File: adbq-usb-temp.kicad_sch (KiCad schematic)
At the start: 72 parts, among them J4 USB_C_Receptacle_USB2.0_14P, Q1 Q_NMOS, Q2 Q_NMOS, Q3 Q_NMOS, SW1 SW_Push, SW2 TestPoint, SW3 TestPoint, SW4 TestPoint, U1 ESP32-S3FH4R2, U14 TMP117AIDRV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

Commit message: schem: run and fix ERC
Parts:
- L1: value L -> 0u47
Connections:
- net DIG1: now also U1.16 (GPIO11/ADC2_CH0)
- net DIG2: now also U1.17 (GPIO12/ADC2_CH1)
- net DIG3: now also U1.18 (GPIO13/ADC2_CH2)

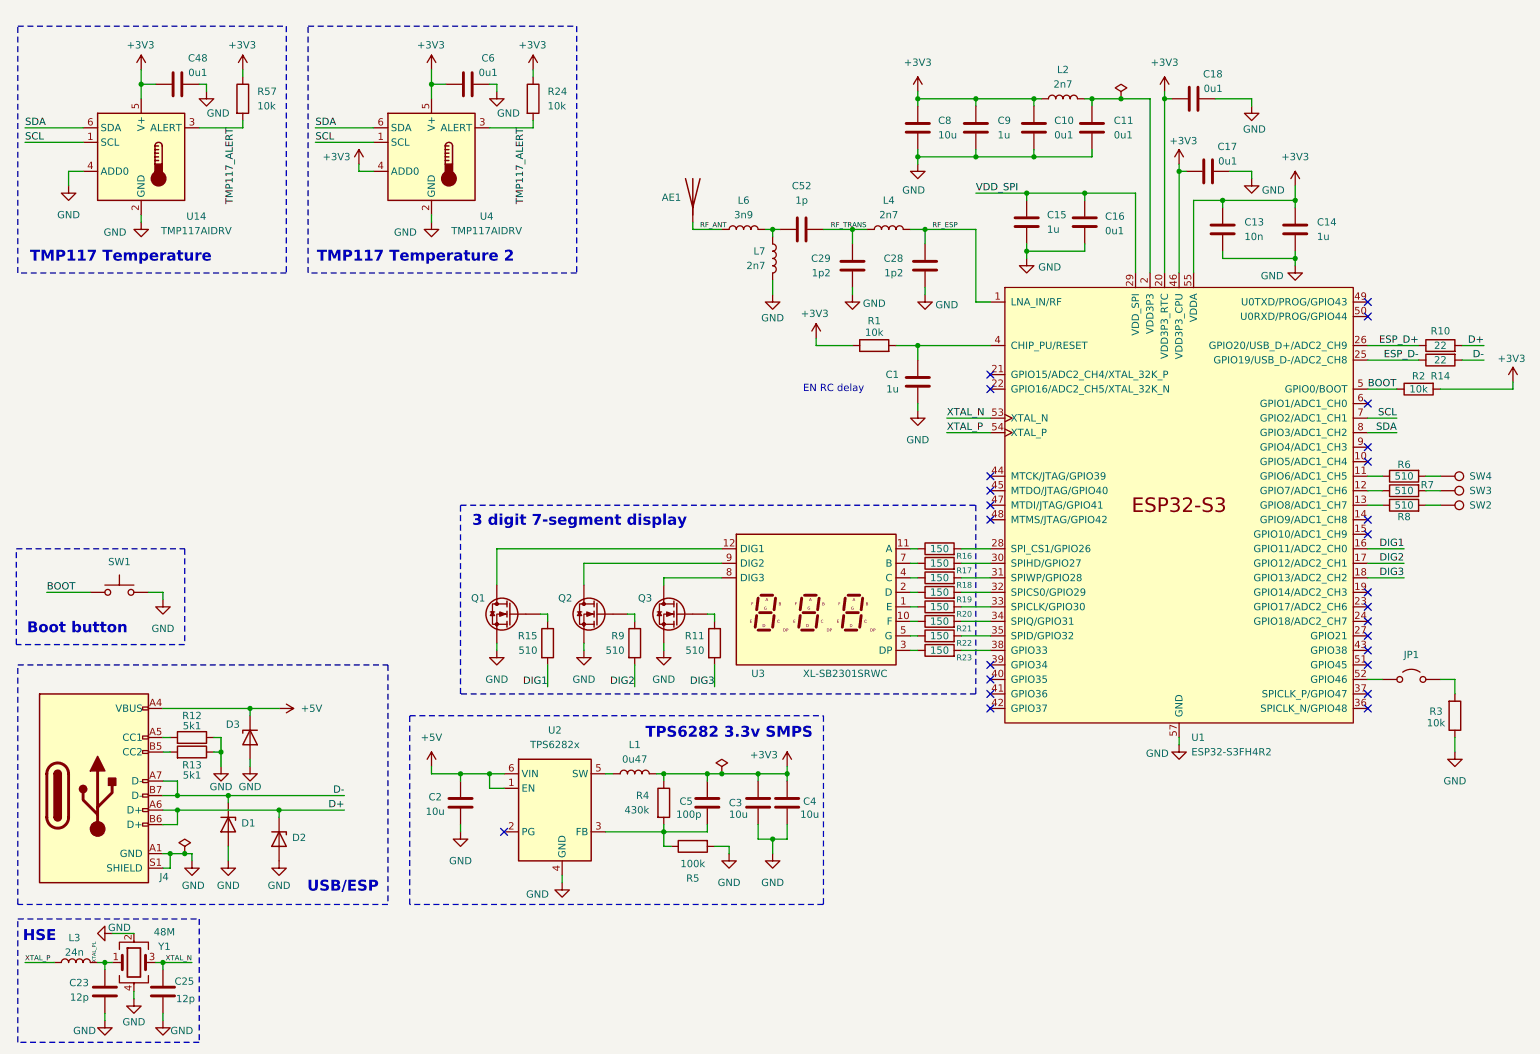
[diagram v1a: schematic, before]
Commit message: schem: add i2c pullup
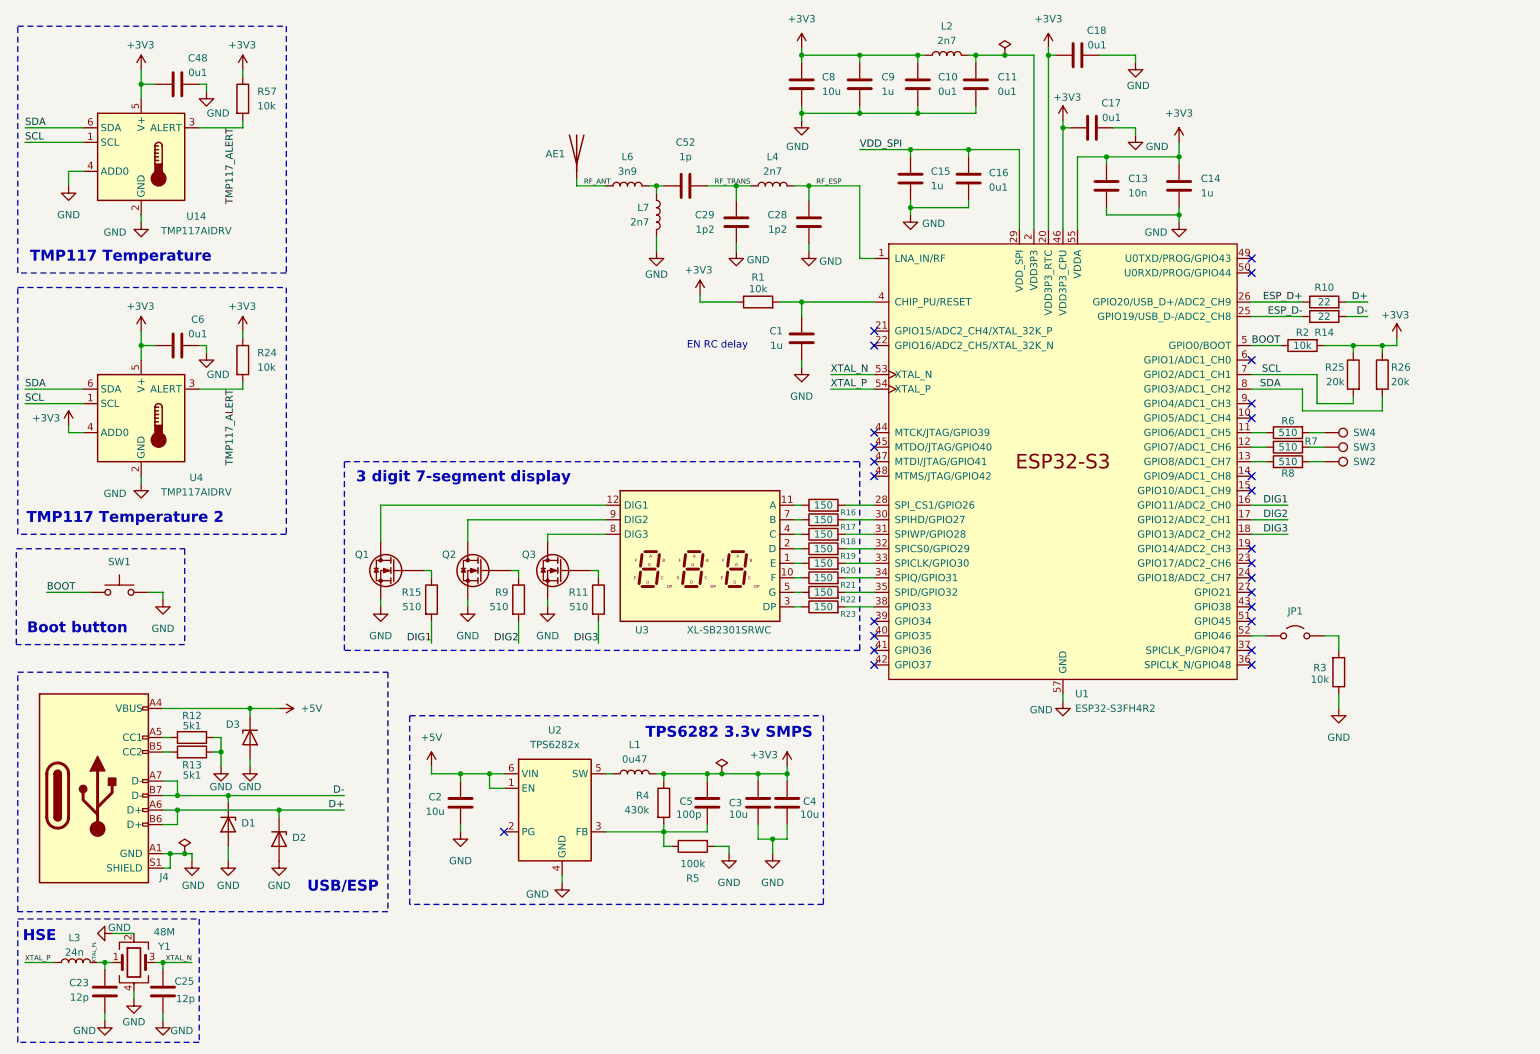
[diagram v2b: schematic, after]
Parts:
- added R25, R26: 20k, symbol Device:R
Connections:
- net +3V3: now also R25.1, R26.1
- net SCL: now also R25.2
- net SDA: now also R26.2
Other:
- moved on the sheet: AE1, C1, C10, C11, C13, C14, C15, C16, C17, C18, C28, C29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

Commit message: schem: connect TMP117 altert pins to MCU
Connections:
- net TMP117_ALERT: now also U1.24 (GPIO18/ADC2_CH7); no longer R24.2, U4.3 (ALERT)
- net TMP117_ALERT_2: now reaches U1.23 (GPIO17/ADC2_CH6)
- net TMP117_ALERT_2: now also R24.2, U4.3 (ALERT)
- no-connect marks 26 -> 24
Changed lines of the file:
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@@
-	)
-	(no_connect
-		(at 232.41 113.03)
 	)
 	(no_connect
@@
 	)
 	(no_connect
-		(at 232.41 110.49)
-	)
-	(no_connect
 		(at 232.41 115.57)
 	)
@@
 	(wire
 		(pts
+			(xy 232.41 113.03) (xy 250.19 113.03)
+		)
+		(stroke
+			(width 0)
+			(type default)
+		)
+	)
+	(wire
+		(pts
 			(xy 49.53 73.66) (xy 49.53 72.39)
 		)
@@
 		(pts
 			(xy 129.54 147.32) (xy 137.16 147.32)
+		)
+		(stroke
+			(width 0)
+			(type default)
+		)
+	)
+	(wire
+		(pts
+			(xy 232.41 110.49) (xy 250.19 110.49)
 		)
 		(stroke
@@
 		)
 	)
+	(label "TMP117_ALERT"
+		(at 250.19 113.03 180)
+		(effects
+			(font
+				(size 1.27 1.27)
+			)
+			(justify right bottom)
+		)
+	)
 	(label "SDA"
 		(at 17.78 80.01 0)
@@
 		)
 	)
+	(label "TMP117_ALERT_2"
+		(at 250.19 110.49 180)
+		(effects
+			(font
+				(size 1.27 1.27)
+			)
+			(justify right bottom)
+		)
+	)
 	(label "DIG1"
 		(at 88.9 124.46 180)
@@
 		)
 	)
-	(label "TMP117_ALERT"
+	(label "TMP117_ALERT_2"
 		(at 54.61 80.01 270)
 		(effects

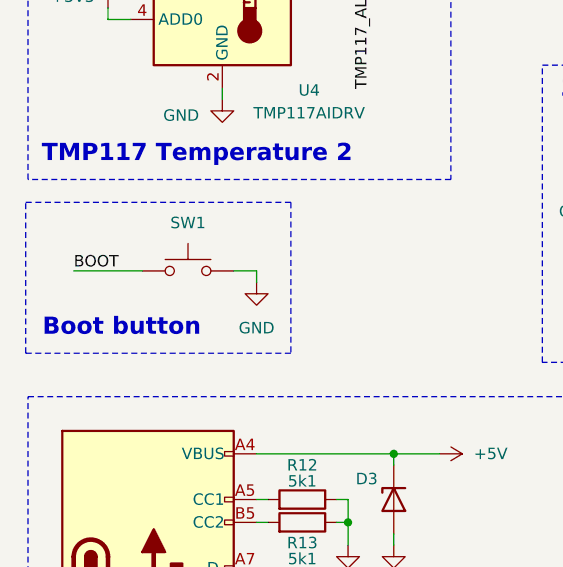
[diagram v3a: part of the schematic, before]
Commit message: schem: add title
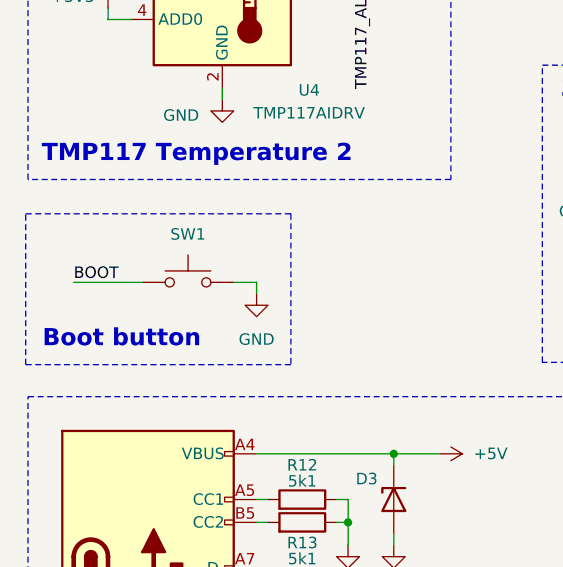
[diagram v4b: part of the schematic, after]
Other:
- company: (none) -> Rémi Ait-Younes
- title: (none) -> ADBQ USB temperature sensor
- moved on the sheet: SW1
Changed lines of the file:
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@@
 	(generator_version "9.0")
 	(paper "A4")
+	(title_block
+		(title "ADBQ USB temperature sensor")
+		(date "2025-11-14")
+		(rev "01")
+		(company "Rémi Ait-Younes")
+	)
 	(rectangle
 		(start 85.09 137.16)
@@
 	)
 	(rectangle
-		(start 16.256 107.95)
-		(end 45.72 124.714)
+		(start 16.256 109.22)
+		(end 45.72 125.984)
 		(stroke
 			(width 0)
@@
 	(text "Boot button"
 		(exclude_from_sim no)
-		(at 26.924 121.92 0)
+		(at 26.924 123.19 0)
 		(effects
 			(font
@@
 	(wire
 		(pts
-			(xy 41.91 115.57) (xy 41.91 116.84)
+			(xy 41.91 116.84) (xy 41.91 118.11)
 		)
 		(stroke
@@
 	(wire
 		(pts
-			(xy 21.59 115.57) (xy 29.21 115.57)
+			(xy 21.59 116.84) (xy 29.21 116.84)
 		)
 		(stroke
@@
 	(wire
 		(pts
-			(xy 41.91 115.57) (xy 39.37 115.57)
+			(xy 41.91 116.84) (xy 39.37 116.84)
 		)
 		(stroke
@@
 	)
 	(label "BOOT"
-		(at 21.59 115.57 0)
+		(at 21.59 116.84 0)
 		(effects
 			(font
@@
 	(symbol
 		(lib_id "Switch:SW_Push")
-		(at 34.29 115.57 0)
+		(at 34.29 116.84 0)
 		(unit 1)
 		(exclude_from_sim no)
@@
 		(dnp no)
 		(property "Reference" "SW1"
-			(at 34.29 110.236 0)
+			(at 34.29 111.506 0)
 			(effects
 				(font
@@
 		)
 		(property "Value" "SW_Push"
-			(at 34.29 110.49 0)
+			(at 34.29 111.76 0)
 			(effects
 				(font
@@
 		)
 		(property "Footprint" ""
-			(at 34.29 110.49 0)
+			(at 34.29 111.76 0)
 			(effects
 				(font
@@
 		)
 		(property "Datasheet" "~"
-			(at 34.29 110.49 0)
+			(at 34.29 111.76 0)
 			(effects
 				(font
@@
 		)
 		(property "Description" "Push button switch, generic, two pins"
-			(at 34.29 115.57 0)
+			(at 34.29 116.84 0)
 			(effects
 				(font
@@
 	(symbol
 		(lib_id "power:GND")
-		(at 41.91 116.84 0)
+		(at 41.91 118.11 0)
 		(unit 1)
 		(exclude_from_sim no)
@@
 		(fields_autoplaced yes)
 		(property "Reference" "#PWR08"
-			(at 41.91 123.19 0)
+			(at 41.91 124.46 0)
 			(effects
 				(font
@@
 		)
 		(property "Value" "GND"
-			(at 41.91 121.92 0)
+			(at 41.91 123.19 0)
 			(effects
 				(font
@@
 		)
 		(property "Footprint" ""
-			(at 41.91 116.84 0)
+			(at 41.91 118.11 0)
 			(effects
 				(font
@@
 		)
 		(property "Datasheet" ""
-			(at 41.91 116.84 0)
+			(at 41.91 118.11 0)
 			(effects
 				(font
@@
 		)
 		(property "Description" "Power symbol creates a global label with name \"GND\" , ground"
-			(at 41.91 116.84 0)
+			(at 41.91 118.11 0)
 			(effects
 				(font

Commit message: schem: assign footprints
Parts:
- C1, C2, C3, C4, C5: footprint (none) -> Capacitor_SMD:C_0402_1005Metric
- JP1, SW1: footprint (none) -> Jumper:SolderJumper-2_P1.3mm_Open_RoundedPad1.0x1.5mm
- L1: footprint (none) -> Pers:TDK_TFM201610ALC
- Q1, Q2, Q3: footprint (none) -> Package_TO_SOT_SMD:SOT-323_SC-70
- R1, R11, R15, R16, R17, R18, R19, R2, R20, R21, R22, R23, R25, R26, R3, R4, R5, R6, R7, R8, R9: footprint (none) -> Resistor_SMD:R_0402_1005Metric
- R12, R13: footprint Resistor_SMD:R_0603_1608Metric -> Resistor_SMD:R_0402_1005Metric
- SW2, SW3, SW4: footprint (none) -> TestPoint:TestPoint_Pad_D1.5mm
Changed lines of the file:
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@@
 			)
 		)
-		(property "Footprint" ""
+		(property "Footprint" "Resistor_SMD:R_0402_1005Metric"
 			(at 87.122 116.84 90)
 			(effects
@@
 			)
 		)
-		(property "Footprint" "Resistor_SMD:R_0603_1608Metric"
+		(property "Footprint" "Resistor_SMD:R_0402_1005Metric"
 			(at 46.99 145.288 90)
 			(effects
@@
 			)
 		)
-		(property "Footprint" ""
+		(property "Footprint" "Resistor_SMD:R_0402_1005Metric"
 			(at 116.332 116.84 90)
 			(effects
@@
 			)
 		)
-		(property "Footprint" ""
+		(property "Footprint" "Resistor_SMD:R_0402_1005Metric"
 			(at 134.62 158.242 90)
 			(effects
@@
 			)
 		)
-		(property "Footprint" ""
+		(property "Footprint" "TestPoint:TestPoint_Pad_D1.5mm"
 			(at 245.11 95.25 0)
 			(effects
@@
 			)
 		)
-		(property "Footprint" ""
+		(property "Footprint" "Resistor_SMD:R_0402_1005Metric"
 			(at 157.48 102.108 90)
 			(effects
@@
 			)
 		)
-		(property "Footprint" ""
+		(property "Footprint" "Jumper:SolderJumper-2_P1.3mm_Open_RoundedPad1.0x1.5mm"
 			(at 34.29 111.76 0)
 			(effects
@@
 			)
 		)
-		(property "Footprint" ""
+		(property "Footprint" "TestPoint:TestPoint_Pad_D1.5mm"
 			(at 245.11 92.71 0)
 			(effects
@@
 			)
 		)
-		(property "Footprint" ""
+		(property "Footprint" "Capacitor_SMD:C_0402_1005Metric"
 			(at 136.1948 156.21 0)
 			(effects
@@
 			)
 		)
-		(property "Footprint" ""
+		(property "Footprint" "Capacitor_SMD:C_0402_1005Metric"
 			(at 94.9452 156.21 0)
 			(effects
@@
 			)
 		)
-		(property "Footprint" ""
+		(property "Footprint" "Resistor_SMD:R_0402_1005Metric"
 			(at 157.48 104.648 90)
 			(effects
@@
 			)
 		)
-		(property "Footprint" "Resistor_SMD:R_0603_1608Metric"
+		(property "Footprint" "Resistor_SMD:R_0402_1005Metric"
 			(at 46.99 142.748 90)
 			(effects
@@
 			)
 		)
-		(property "Footprint" ""
+		(property "Footprint" "Resistor_SMD:R_0402_1005Metric"
 			(at 245.872 129.54 90)
 			(effects
@@
 			)
 		)
-		(property "Footprint" ""
+		(property "Footprint" "Package_TO_SOT_SMD:SOT-323_SC-70"
 			(at 106.68 109.22 0)
 			(effects
@@
 			)
 		)
-		(property "Footprint" ""
+		(property "Footprint" "Resistor_SMD:R_0402_1005Metric"
 			(at 157.48 112.268 90)
 			(effects
@@
 			)
 		)
-		(property "Footprint" ""
+		(property "Footprint" "Resistor_SMD:R_0402_1005Metric"
 			(at 146.05 66.548 90)
 			(effects
@@
 			)
 		)
-		(property "Footprint" ""
+		(property "Footprint" "Resistor_SMD:R_0402_1005Metric"
 			(at 157.48 107.188 90)
 			(effects
@@
 			)
 		)
-		(property "Footprint" ""
+		(property "Footprint" "Resistor_SMD:R_0402_1005Metric"
 			(at 157.48 109.728 90)
 			(effects
@@
 			)
 		)
-		(property "Footprint" ""
+		(property "Footprint" "Resistor_SMD:R_0402_1005Metric"
 			(at 157.48 119.888 90)
 			(effects
@@
 			)
 		)
-		(property "Footprint" ""
+		(property "Footprint" "Pers:TDK_TFM201610ALC"
 			(at 124.46 147.32 0)
 			(effects
@@
 			)
 		)
-		(property "Footprint" ""
+		(property "Footprint" "Package_TO_SOT_SMD:SOT-323_SC-70"
 			(at 77.47 109.22 0)
 			(effects
@@
 			)
 		)
-		(property "Footprint" ""
+		(property "Footprint" "Resistor_SMD:R_0402_1005Metric"
 			(at 127.762 152.4 90)
 			(effects
@@
 			)
 		)
-		(property "Footprint" ""
+		(property "Footprint" "Resistor_SMD:R_0402_1005Metric"
 			(at 238.76 94.488 90)
 			(effects
@@
 			)
 		)
-		(property "Footprint" ""
+		(property "Footprint" "Resistor_SMD:R_0402_1005Metric"
 			(at 157.48 114.808 90)
 			(effects
@@
 			)
 		)
-		(property "Footprint" ""
+		(property "Footprint" "TestPoint:TestPoint_Pad_D1.5mm"
 			(at 245.11 97.79 0)
 			(effects
@@
 			)
 		)
-		(property "Footprint" ""
+		(property "Footprint" "Resistor_SMD:R_0402_1005Metric"
 			(at 238.76 85.852 90)
 			(effects
@@
 			)
 		)
-		(property "Footprint" ""
+		(property "Footprint" "Package_TO_SOT_SMD:SOT-323_SC-70"
 			(at 92.71 109.22 0)
 			(effects
@@
 			)
 		)
-		(property "Footprint" ""
+		(property "Footprint" "Jumper:SolderJumper-2_P1.3mm_Open_RoundedPad1.0x1.5mm"
 			(at 240.03 123.19 0)
 			(effects
@@
 			)
 		)
-		(property "Footprint" ""
+		(property "Footprint" "Resistor_SMD:R_0402_1005Metric"
 			(at 157.48 117.348 90)
 			(effects
@@
 			)
 		)
-		(property "Footprint" ""
+		(property "Footprint" "Capacitor_SMD:C_0402_1005Metric"
 			(at 152.0952 156.21 0)
 			(effects
@@
 			)
 		)
-		(property "Footprint" ""
+		(property "Footprint" "Resistor_SMD:R_0402_1005Metric"
 			(at 102.362 116.84 90)
 			(effects
@@
 			)
 		)
-		(property "Footprint" ""
+		(property "Footprint" "Capacitor_SMD:C_0402_1005Metric"
 			(at 152.7048 74.93 0)
 			(effects
@@
 			)
 		)
-		(property "Footprint" ""
+		(property "Footprint" "Resistor_SMD:R_0402_1005Metric"
 			(at 241.3 70.612 90)
 			(effects
@@
 			)
 		)
-		(property "Footprint" ""
+		(property "Footprint" "Resistor_SMD:R_0402_1005Metric"
 			(at 253.492 77.47 90)
 			(effects
@@
 			)
 		)
-		(property "Footprint" ""
+		(property "Footprint" "Resistor_SMD:R_0402_1005Metric"
 			(at 238.76 88.392 90)
 			(effects
@@
 			)
 		)
-		(property "Footprint" ""
+		(property "Footprint" "Resistor_SMD:R_0402_1005Metric"
 			(at 251.968 77.47 90)
 			(effects
@@
 			)
 		)
-		(property "Footprint" ""
+		(property "Footprint" "Capacitor_SMD:C_0402_1005Metric"
 			(at 145.0848 156.21 0)
 			(effects

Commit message: schem: add part numbers
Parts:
- C1: Basic (none) -> Y; JLCPCB Part # (none) -> C52923; Manufacturer (none) -> Samsung Electro-Mechanics; Manufacturer Part Number (none) -> CL05A105KA5NQNC
- C2, C3, C4: Basic (none) -> Y; JLCPCB Part # (none) -> C15525; Manufacturer (none) -> Samsung Electro-Mechanics; Manufacturer Part Number (none) -> CL05A106MQ5NUNC
- C5: Basic (none) -> Y; JLCPCB Part # (none) -> C1546; Manufacturer (none) -> Guangdong Fenghua Advanced Tech (FH); Manufacturer Part Number (none) -> 0402CG101J500NT
- D1, D2, D3: Basic (none) -> E; JLCPCB Part # (none) -> C22395519; Manufacturer (none) -> hongjiacheng; Manufacturer Part Number (none) -> H5VU10U
- JP1, SW1, SW2, SW3, SW4, U3: now left out of the parts list
- L1: Basic (none) -> X; JLCPCB Part # (none) -> C2045043; Manufacturer (none) -> TDK; Manufacturer Part Number (none) -> TFM201610ALC-R47MTAA
- L2, L4: JLCPCB Part # C412269 -> C77108; Manufacturer Part Number LQW15AN2N7G80D -> LQG15HS2N7S02D
- L7: Basic (none) -> X
- Q1, Q2, Q3: Basic (none) -> E; JLCPCB Part # (none) -> C28646265; Manufacturer (none) -> hongjiacheng; Manufacturer Part Number (none) -> BSS138W
- R1, R2, R3: Basic (none) -> Y; JLCPCB Part # (none) -> C25804; Manufacturer (none) -> Uniroyal Elec; Manufacturer Part Number (none) -> 0603WAF1002T5E
- R11, R15, R6, R7, R8, R9: Basic (none) -> Y; JLCPCB Part # (none) -> C25123; Manufacturer (none) -> Uniroyal Elec; Manufacturer Part Number (none) -> 0402WGF5100TCE
- R16, R17, R18, R19, R20, R21, R22, R23: Basic (none) -> Y; JLCPCB Part # (none) -> C25082; Manufacturer (none) -> Uniroyal Elec; Manufacturer Part Number (none) -> 0402WGF1500TCE
- R25, R26: Basic (none) -> Y; JLCPCB Part # (none) -> C25765; Manufacturer (none) -> Uniroyal Elec; Manufacturer Part Number (none) -> 0402WGF2002TCE
- R4: footprint Resistor_SMD:R_0402_1005Metric -> Resistor_SMD:R_0603_1608Metric; Basic (none) -> E; JLCPCB Part # (none) -> C25969; Manufacturer (none) -> Uniroyal Elec; Manufacturer Part Number (none) -> 0603WAF4303T5E
- R5: Basic (none) -> Y; JLCPCB Part # (none) -> C25741; Manufacturer (none) -> Uniroyal Elec; Manufacturer Part Number (none) -> 0402WGF1003TCE
- U1: Basic (none) -> X; JLCPCB Part # (none) -> C3013940; Manufacturer (none) -> Espressif; Manufacturer Part Number (none) -> ESP32-S3FH4R2
- U2: Basic (none) -> X; JLCPCB Part # (none) -> C2650334; Manufacturer (none) -> Texas Instruments; Manufacturer Part Number (none) -> TPS62825DMQR
